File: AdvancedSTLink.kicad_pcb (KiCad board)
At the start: 4 copper layers, 49.9 x 23.1 mm, 60 parts, among them J1 USB_C_Receptacle, J2 Conn_02x03_Odd_Even, J3 Conn_01x06, J4 Conn_02x03_Odd_Even, Q1 S8050, SW1 SW_SPDT, U1 STM32F205RETx, U2 XC6206P332MR, U3 USBLC6-2P6, U4 GM9038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

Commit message: Fix a wire.
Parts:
- moved SW1 0.36 mm to (182.0, 100.4)
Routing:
- net VBUS: track 36.2 -> 36.8 mm
- net Net-(D6-Pad2): track 8.66 -> 8.13 mm
- net TCK1: track 17.4 -> 17.9 mm

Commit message: Add teardrops
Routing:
- net GND: track 59.8 -> 58.8 mm
- net USB_DN: track 18.0 -> 17.5 mm

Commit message: Update.
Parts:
- added C19: 4.7uF, Capacitor_SMD:C_0603_1608Metric, F.Cu at (209.1, 110.0)
- added G***: LOGO, logo:onmark, F.Cu at (177.9, 98.1)
- added H7: SMTFixingHole, lc:SMTFixingHole, F.Cu at (164.6, 106.8)
- added H8: SMTFixingHole, lc:SMTFixingHole, F.Cu at (164.7, 90.3)
- added H9: SMTFixingHole, lc:SMTFixingHole, F.Cu at (204.0, 90.4)
- added LOGO: LOGO, logo:logo, B.Cu at (182.3, 106.5)
- added R10: 1.5k, Resistor_SMD:R_0402_1005Metric, F.Cu at (198.4, 99.4)
- added T0: LOGO, logo:pinmark, F.Cu at (205.6, 104.5)
- C12, C17, C6: footprint Capacitor_SMD:C_0603_1608Metric -> Capacitor_SMD:C_0805_2012Metric
- H1, H2, H3, H4: footprint MountingHole:MountingHole_2.5mm -> MountingHole:MountingHole_2.2mm_M2_DIN965
- L1, L2: footprint Inductor_SMD:L_TDK_NLV25_2.5x2.0mm -> lc:DFE252012P
- R16, R8: value 2.2k -> 3.3k
- R6: value 10k -> 2.2k
- R7: value 2.2k -> 3.9k
- U3, U5, U6: footprint Package_TO_SOT_SMD:SOT-666 -> lc:SOT-666
- moved C16 0.89 mm to (209.1, 108.5)
- moved R1 0.62 mm to (182.2, 105.2), turned to 90 degrees
- moved J2 0.50 mm to (183.3, 98.7)
- moved C17 0.46 mm to (188.2, 104.5)
- moved SW1 0.37 mm to (182.0, 100.0)
- moved U5 0.28 mm to (193.7, 99.2), turned to 0 degrees
- moved L2 0.27 mm to (188.4, 107.5)
- moved U6 0.27 mm to (193.7, 101.6), turned to 0 degrees
- moved C12 0.24 mm to (188.1, 110.5)
- moved C5 0.19 mm to (190.6, 105.7)
- moved L1 0.15 mm to (185.8, 107.5)
- moved D3 0.12 mm to (178.5, 108.1)
- moved C6 0.11 mm to (181.8, 110.6)
- moved R15 0.07 mm to (184.0, 110.7)
- turned U3 to 0 degrees
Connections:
- Q1 pad 1: RST_PULL -> Net-(Q1-Pad1)
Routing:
- net Net-(J1-PadA5): track 22.1 -> 6.83 mm, vias 2 -> 0
- net Net-(J1-PadB5): track 20.8 -> 7.60 mm
- net Net-(Q1-Pad1): track 0.00 -> 11.9 mm, vias 0 -> 2
- net T_NRST_O: track 35.0 -> 25.8 mm, vias 3 -> 2
- net +3V3: track 70.9 -> 78.4 mm, vias 8 -> 9
- net Net-(D6-Pad2): track 8.13 -> 5.63 mm, vias 2 -> 1
- net Net-(R9-Pad2): track 12.3 -> 9.93 mm
- net RST_PULL: track 7.89 -> 6.26 mm, vias 1 -> 2
- net STM_NRST: track 27.9 -> 26.4 mm
- net V_OUT_3.3: track 42.7 -> 44.0 mm
- net STM_SWCLK: track 10.2 -> 9.19 mm
- net GND: track 58.8 -> 59.7 mm, vias 42 -> 40
- net TDO: track 21.2 -> 20.3 mm
- net USB_DP: track 19.3 -> 18.5 mm
- net Net-(C12-Pad1): track 9.14 -> 9.90 mm
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- added copper zone on F.Cu, net Net-(C6-Pad1)
- added copper zone on F.Cu, net Net-(L1-Pad1)
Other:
- board text added: "20-25"
- board text added: "JLCJLCJLC JLCJLC"
- board text added: "Rev. A"
- board text removed: "20-24"

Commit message: Production.
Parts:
- R10: value 1.5k -> 4.7k
- moved C15 0.72 mm to (202.8, 104.5), turned to 180 degrees
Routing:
- net GND: track 59.7 -> 61.0 mm, vias 40 -> 39
- net V_OUT_3.3: track 44.0 -> 45.1 mm

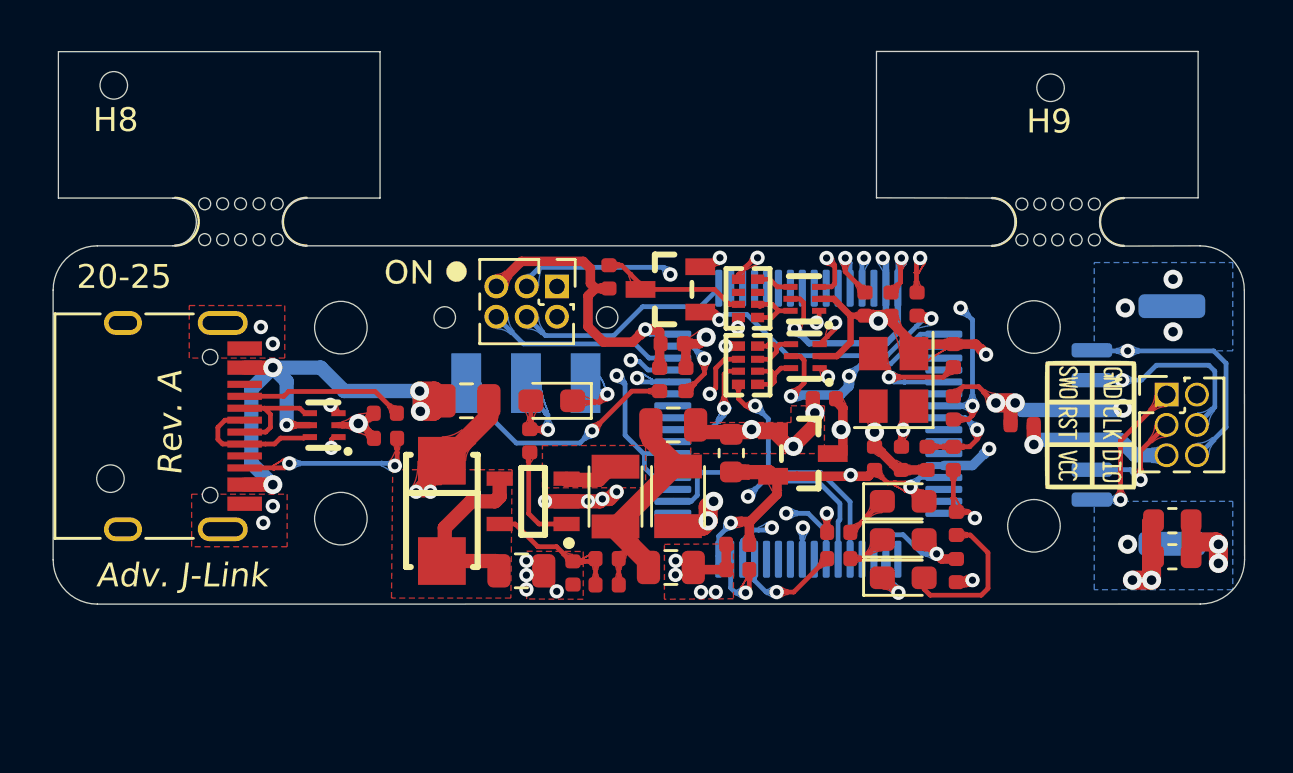
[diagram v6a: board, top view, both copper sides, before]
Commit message: Change pins to 2.54, Add CH340
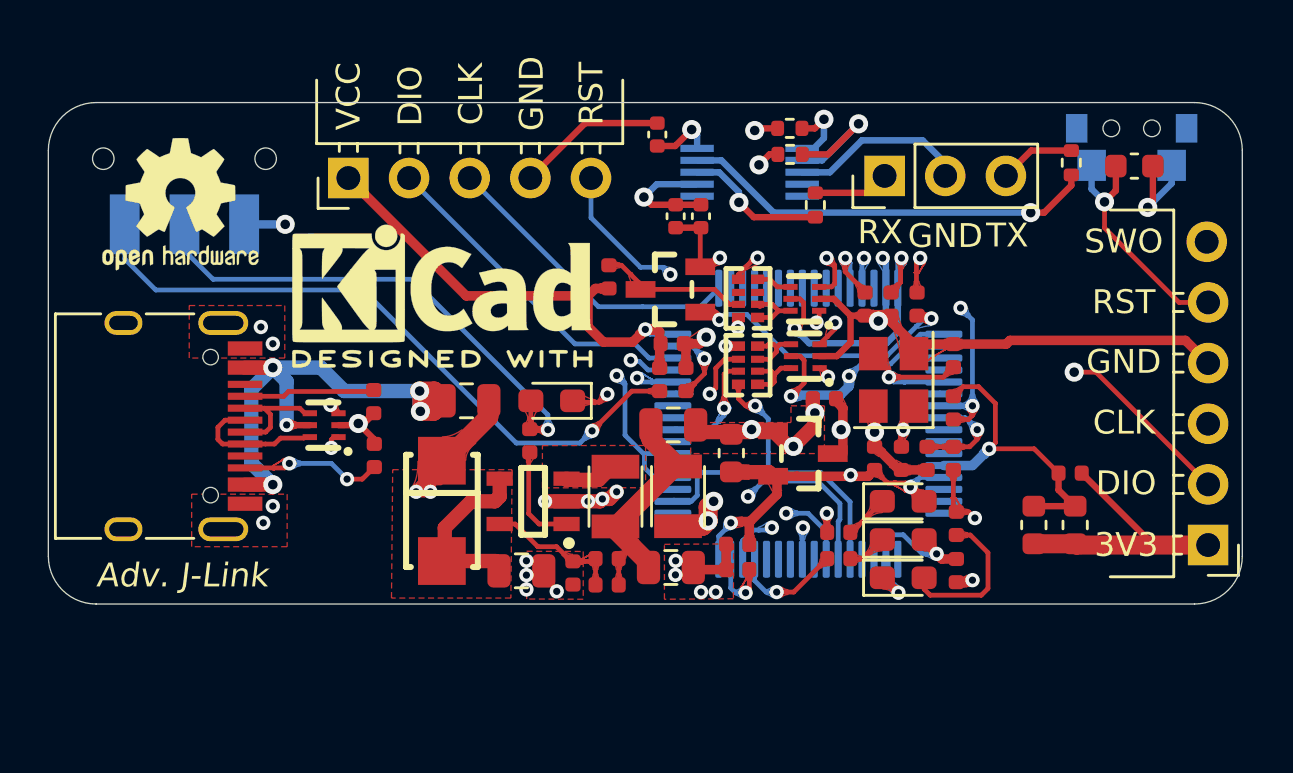
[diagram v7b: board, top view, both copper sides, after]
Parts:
- removed the G*** at (177.9, 98.1)
- removed H1, H2, H3, H4: MountingHole, MountingHole:MountingHole_2.2mm_M2_DIN965
- removed H5, H6: MouseBite, mouse_bite:mouse-bite-3mm-slot
- removed H7, H8, H9: SMTFixingHole, lc:SMTFixingHole
- removed J2: Conn_02x03_Odd_Even, Connector_PinHeader_1.27mm:PinHeader_2x03_P1.27mm_Vertical
- removed LOGO: LOGO, logo:logo
- removed T0: LOGO, logo:pinmark
- added C20: 100nf, Capacitor_SMD:C_0402_1005Metric, F.Cu at (187.5, 92.3)
- added C21: 100nf, Capacitor_SMD:C_0402_1005Metric, F.Cu at (189.3, 95.8)
- added C22: 100nf, Capacitor_SMD:C_0402_1005Metric, F.Cu at (188.3, 95.8)
- added C23: 0.1uF/50V, Capacitor_SMD:C_0603_1608Metric, F.Cu at (207.5, 93.7)
- added G***: LOGO, KisonCommon:HexManLogo, B.Cu at (178.7, 99.4)
- added J5: Conn_01x05, KisonNew:JLinkDebugSWD, F.Cu at (174.6, 94.2)
- added R11: 22, Resistor_SMD:R_0402_1005Metric, F.Cu at (193.1, 92.1)
- added R12: 22, Resistor_SMD:R_0402_1005Metric, F.Cu at (193.1, 93.2)
- added R13: 100, Resistor_SMD:R_0402_1005Metric, F.Cu at (194.1, 95.3)
- added R18: 100, Resistor_SMD:R_0402_1005Metric, F.Cu at (204.8, 93.5)
- added REF**: KiCad-Logo2_5mm_SilkScreen, Symbol:KiCad-Logo2_5mm_SilkScreen, F.Cu at (178.5, 99.1)
- added REF**: OSHW-Logo2_7.3x6mm_SilkScreen, Symbol:OSHW-Logo2_7.3x6mm_SilkScreen, F.Cu at (167.5, 95.2)
- added SW2: SW_Push, KisonNew:C393942, B.Cu at (207.4, 92.9)
- added U7: CH340E, Package_SO:MSOP-10_3x3mm_P0.5mm, B.Cu at (191.4, 93.9)
- J1: value USB_C_Receptacle -> Conn_01x03; footprint Connector_USB:USB_C_Receptacle_HRO_TYPE-C-31-M-12 -> Connector_PinHeader_2.54mm:PinHeader_1x03_P2.54mm_Vertical
- J3: footprint Connector_Molex:Molex_CLIK-Mate_502382-0670_1x06-1MP_P1.25mm_Vertical -> KisonNew:JLinkDebugSWDO; moved to F.Cu
- J4: value Conn_02x03_Odd_Even -> USB_C_Receptacle_USB2.0; footprint Connector_PinHeader_1.27mm:PinHeader_2x03_P1.27mm_Vertical -> Connector_USB:USB_C_Receptacle_HRO_TYPE-C-31-M-12
- moved J4 42.7 mm to (166.2, 104.5), turned to -90 degrees
- moved J1 32.6 mm to (197.0, 94.1), turned to 90 degrees
- moved SW1 15.8 mm to (167.7, 93.3)
- moved C19 5.95 mm to (203.3, 108.7), turned to 90 degrees
- moved J3 5.82 mm to (210.6, 109.5), turned to 180 degrees
- moved C16 4.07 mm to (205.0, 108.7), turned to 90 degrees
- moved C15 2.86 mm to (204.8, 106.5)
- moved R5 0.86 mm to (175.7, 105.8), turned to -90 degrees
- moved R4 0.69 mm to (175.6, 103.5), turned to 90 degrees
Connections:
- FB1 pad 2: Net-(FB1-Pad2) -> Net-(U3-VBUS)
- J3 pad 1: T_SWO_O -> V_OUT_3.3
- J3 pad 2: T_NRST_O -> T_SWDIO_O
- J3 pad 3: V_OUT_3.3 -> T_SWCLK_O
- J3 pad 5: T_SWCLK_O -> T_NRST_O
- J3 pad 6: T_SWDIO_O -> T_SWO_O
- R4 pad 2: Net-(J1-PadA5) -> Net-(J4-CC1)
- R5 pad 2: Net-(J1-PadB5) -> Net-(J4-CC2)
- RN2 pad 3: Net-(RN2-Pad3) -> unconnected-(RN2-R3.1-Pad3)
- RN2 pad 6: Net-(RN2-Pad6) -> unconnected-(RN2-R3.2-Pad6)
- U1 pad 10: Net-(U1-Pad10) -> unconnected-(U1-PC2-Pad10)
- U1 pad 11: Net-(U1-Pad11) -> unconnected-(U1-PC3-Pad11)
- U1 pad 14: Net-(U1-Pad14) -> unconnected-(U1-PA0-Pad14)
- U1 pad 15: Net-(U1-Pad15) -> unconnected-(U1-PA1-Pad15)
- U1 pad 16: Net-(U1-Pad16) -> unconnected-(U1-PA2-Pad16)
- U1 pad 17: Net-(U1-Pad17) -> unconnected-(U1-PA3-Pad17)
- U1 pad 2: Net-(U1-Pad2) -> unconnected-(U1-PC13-Pad2)
- U1 pad 20: Net-(U1-Pad20) -> unconnected-(U1-PA4-Pad20)
- U1 pad 24: Net-(U1-Pad24) -> unconnected-(U1-PC4-Pad24)
- U1 pad 26: Net-(U1-Pad26) -> unconnected-(U1-PB0-Pad26)
- U1 pad 27: Net-(U1-Pad27) -> unconnected-(U1-PB1-Pad27)
- U1 pad 28: Net-(U1-Pad28) -> unconnected-(U1-PB2-Pad28)
- U1 pad 3: Net-(U1-Pad3) -> unconnected-(U1-PC14-Pad3)
- U1 pad 33: Net-(U1-Pad33) -> unconnected-(U1-PB12-Pad33)
- U1 pad 35: Net-(U1-Pad35) -> unconnected-(U1-PB14-Pad35)
- U1 pad 39: Net-(U1-Pad39) -> unconnected-(U1-PC8-Pad39)
- U1 pad 4: Net-(U1-Pad4) -> unconnected-(U1-PC15-Pad4)
- U1 pad 41: Net-(U1-Pad41) -> unconnected-(U1-PA8-Pad41)
- U1 pad 42: Net-(U1-Pad42) -> unconnected-(U1-PA9-Pad42)
- U1 pad 50: Net-(U1-Pad50) -> unconnected-(U1-PA15-Pad50)
- U1 pad 51: Net-(U1-Pad51) -> unconnected-(U1-PC10-Pad51)
- U1 pad 52: Net-(U1-Pad52) -> unconnected-(U1-PC11-Pad52)
- U1 pad 53: Net-(U1-Pad53) -> unconnected-(U1-PC12-Pad53)
- U1 pad 54: Net-(U1-Pad54) -> unconnected-(U1-PD2-Pad54)
- U1 pad 55: Net-(U1-Pad55) -> unconnected-(U1-PB3-Pad55)
- U1 pad 56: Net-(U1-Pad56) -> unconnected-(U1-PB4-Pad56)
- U1 pad 57: Net-(U1-Pad57) -> unconnected-(U1-PB5-Pad57)
- U1 pad 58: Net-(U1-Pad58) -> unconnected-(U1-PB6-Pad58)
- U1 pad 59: Net-(U1-Pad59) -> unconnected-(U1-PB7-Pad59)
- U1 pad 62: Net-(U1-Pad62) -> unconnected-(U1-PB9-Pad62)
- U1 pad 9: Net-(U1-Pad9) -> unconnected-(U1-PC1-Pad9)
- U3 pad 5: Net-(FB1-Pad2) -> Net-(U3-VBUS)
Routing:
- net VBUS: track 36.5 -> 68.0 mm, vias 3 -> 4
- net GND: track 61.0 -> 87.9 mm, vias 39 -> 31
- net USB_DP: track 18.5 -> 45.0 mm, vias 2 -> 3
- net Net-(U3-VBUS): track 0.00 -> 23.5 mm, vias 0 -> 5
- net Net-(FB1-Pad2): track 23.5 -> 0.00 mm, vias 5 -> 0
- net USB_DN: track 17.2 -> 40.2 mm, vias 2 -> 3
- net Net-(SW1-A): track 9.93 -> 27.9 mm
- net Net-(U7-RXD): track 0.00 -> 17.5 mm, vias 0 -> 1
- net Net-(D6-A): track 5.63 -> 21.9 mm
- net Net-(J1-PadB5): track 7.60 -> 0.00 mm, vias 2 -> 0
- net T_SWO_O: track 26.4 -> 19.4 mm, vias 2 -> 1
- net Net-(J1-PadA5): track 6.83 -> 0.00 mm
- net +3V3: track 78.4 -> 85.1 mm
- net STM_SWDIO: track 8.11 -> 14.2 mm
- net Net-(J4-CC2): track 0.00 -> 5.99 mm, vias 0 -> 2
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- added copper zone on F.Cu, net Net-(U3-VBUS)
- removed copper zone on B.Cu, net GND
- removed copper zone on F.Cu, net Net-(FB1-Pad2)
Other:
- board size 49.9 x 23.1 mm -> 50 x 21 mm
- net class Default removed
- rule pad_to_mask_clearance: 0.051 -> 0
- board text added: "GND"
- board text added: "RX"
- board text added: "TX"
- board text removed: "20-25"
- board text removed: "Rev. A"

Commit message: Remove CH340, use VCOM
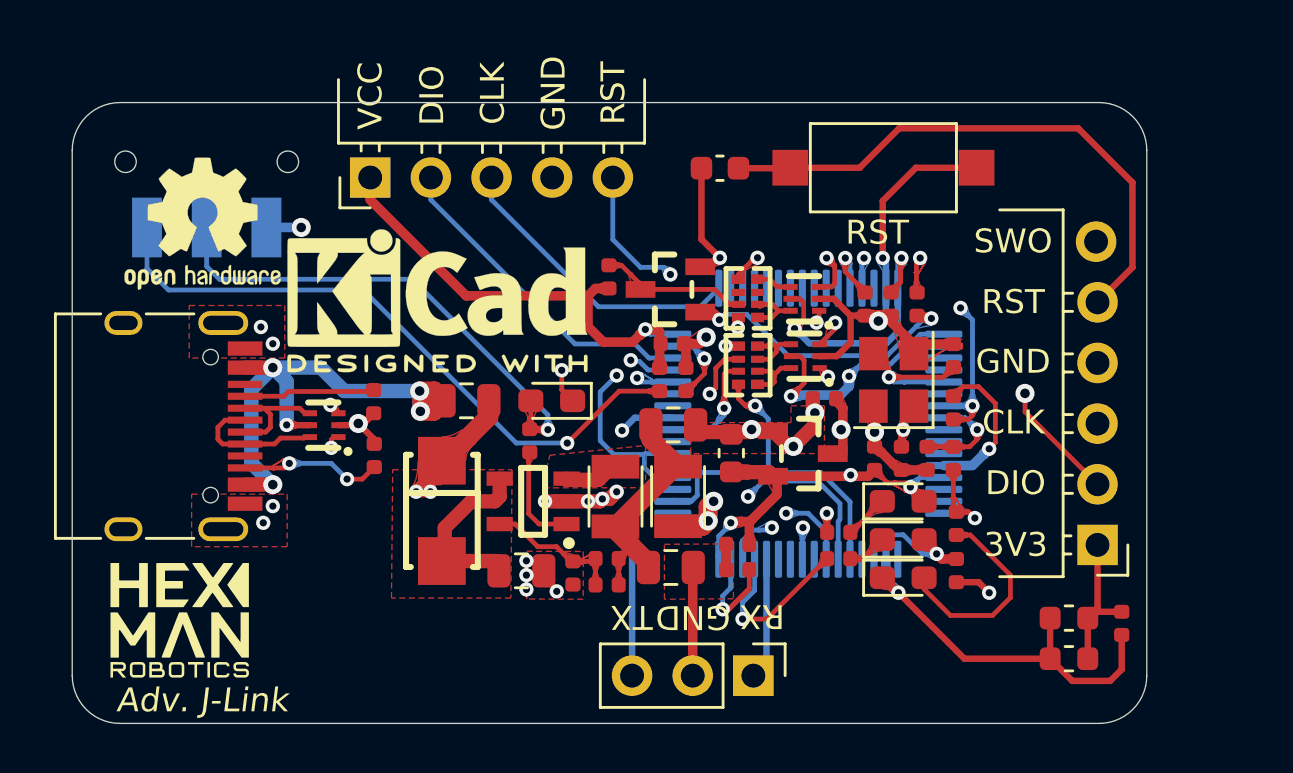
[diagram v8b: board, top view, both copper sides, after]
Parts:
- removed C20, C21, C22: 100nf, Capacitor_SMD:C_0402_1005Metric
- removed R11, R12: 22, Resistor_SMD:R_0402_1005Metric
- removed R13, R18: 100, Resistor_SMD:R_0402_1005Metric
- removed U7: CH340E, Package_SO:MSOP-10_3x3mm_P0.5mm
- added G***: LOGO, KisonCommon:HexManLogoBig, B.Cu at (178.1, 111.7)
- G***: moved to F.Cu
- SW2: footprint KisonNew:C393942 -> Button_Switch_SMD:SW_SPST_CK_RS282G05A3; moved to F.Cu
- moved J1 21.6 mm to (191.5, 115.0), turned to -90 degrees
- moved C23 17.4 mm to (190.1, 93.8), turned to 180 degrees
- moved G*** 17.3 mm to (167.5, 112.7), turned to 0 degrees
- moved SW2 10.4 mm to (197.0, 93.7)
- moved C15 6.65 mm to (206.9, 112.8), turned to -90 degrees
- moved C19 5.79 mm to (204.7, 114.3), turned to 180 degrees
- moved J3 4.63 mm to (205.9, 109.5)
- moved C16 3.91 mm to (204.7, 112.6), turned to 180 degrees
- moved REF** 1.24 mm to (168.5, 96.1)
- moved SW1 0.94 mm to (168.6, 93.5)
- moved J5 0.92 mm to (175.5, 94.1)
- moved REF** 0.28 mm to (178.3, 99.3)
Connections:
- J1 pad 1: /UART1_RX -> VCOM-JLinkRX
- J1 pad 3: /UART1_TX -> VCOM-JLinkTX
- U1 pad 28: unconnected-(U1-PB2-Pad28) -> VCOM-JLinkRX
- U1 pad 35: unconnected-(U1-PB14-Pad35) -> VCOM-JLinkTX
- U1 pad 41: unconnected-(U1-PA8-Pad41) -> VCOM-JLinkTX
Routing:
- net VBUS: track 68.0 -> 37.7 mm, vias 4 -> 3
- net USB_DP: track 45.0 -> 18.5 mm, vias 3 -> 2
- net USB_DN: track 40.2 -> 17.2 mm, vias 3 -> 2
- net VCOM-JLinkTX: track 0.00 -> 22.8 mm, vias 0 -> 1
- net Net-(U7-RXD): track 17.5 -> 0.00 mm, vias 1 -> 0
- net V_OUT_3.3: track 45.2 -> 32.5 mm
- net GND: track 87.9 -> 77.8 mm, vias 31 -> 26
- net T_NRST_O: track 28.6 -> 37.6 mm, vias 2 -> 1
- net Net-(U7-TXD): track 5.98 -> 0.00 mm, vias 1 -> 0
- net Net-(U7-UD-): track 5.88 -> 0.00 mm, vias 1 -> 0
- net VCOM-JLinkRX: track 0.00 -> 5.10 mm
- net T_SWCLK_O: track 17.2 -> 12.6 mm
- net T_SWO_O: track 19.4 -> 14.7 mm
- net T_SWDIO_O: track 19.6 -> 15.4 mm
- net /UART1_RX: track 3.19 -> 0.00 mm
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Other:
- board size 50 x 21 mm -> 45 x 26 mm
- board text added: "RST"
